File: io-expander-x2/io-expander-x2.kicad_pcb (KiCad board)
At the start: 2 copper layers, 50 x 100 mm, 6 parts, among them IC1 MCP23017-E_SO, IC2 MCP23017-E_SO, J1 CONN4_BM04B-SRSS_JST, J2 CONN4_BM04B-SRSS_JST, J3 Screw-8P-5.08-1729186, J4 Screw-8P-5.08-1729186

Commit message: Daughter board is coming along nicely.
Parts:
- added D1: LED, LED_SMD:LED_1206_3216Metric, F.Cu at (61.1, 43.2)
- added F1: MF-USHT010KX-2, 00_General:FUSC3226X85N, F.Cu at (47.4, 43.2)
- added H1: MountingHole, MountingHole:MountingHole_3.2mm_M3_ISO7380, F.Cu at (45.0, 34.3)
- added H2: MountingHole, MountingHole:MountingHole_3.2mm_M3_ISO7380, F.Cu at (64.8, 34.3)
- added H3: MountingHole, MountingHole:MountingHole_3.2mm_M3_ISO7380, F.Cu at (45.0, 125.7)
- added H4: MountingHole, MountingHole:MountingHole_3.2mm_M3_ISO7380, F.Cu at (64.8, 125.7)
- added J5: Screw-8P-5.08-1729186, 00_Connectors:Screw-8P-5.08-1729186, F.Cu at (36.0, 85.0)
- added J6: Screw-8P-5.08-1729186, 00_Connectors:Screw-8P-5.08-1729186, F.Cu at (73.7, 120.6)
- added R1: R, Resistor_SMD:R_0805_2012Metric, F.Cu at (54.4, 43.2)
- IC1, IC2: footprint 00_General:SOIC127P1030X265-28N -> SamacSys_Parts:SOIC127P1030X265-28N
- moved J2 40.2 mm to (62.8, 80.2)
- moved J3 35.3 mm to (36.0, 39.0)
- moved J4 33.9 mm to (73.7, 73.6)
- moved J1 24.7 mm to (50.1, 80.2), turned to -90 degrees
- moved IC1 22.7 mm to (55.3, 59.0)
- moved IC2 19.8 mm to (55.3, 102.0)
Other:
- board text added: "Port A"
- board text added: "Port B"

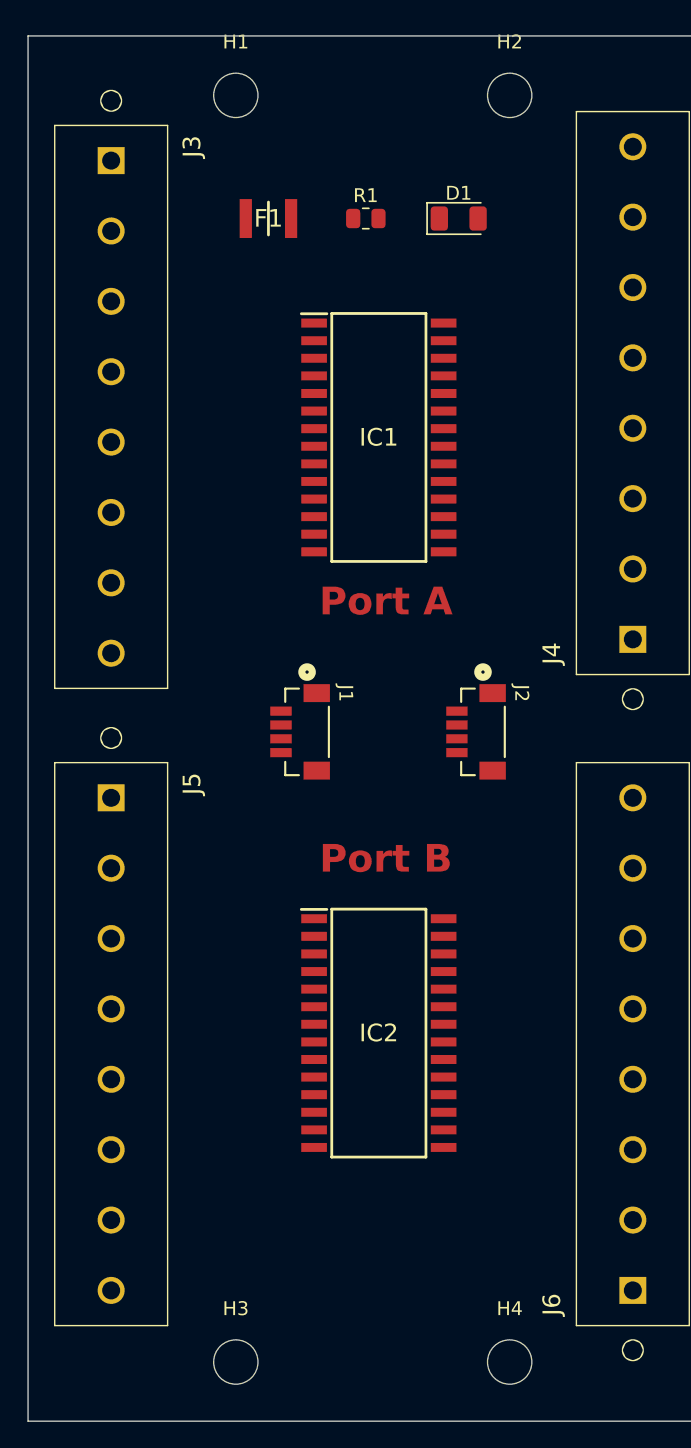
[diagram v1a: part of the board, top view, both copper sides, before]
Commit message: Most components are now placed. The schematic has a lot of the wiring done. Need to transfer it onto the PCB once I figure out how I will wire up the address lines.
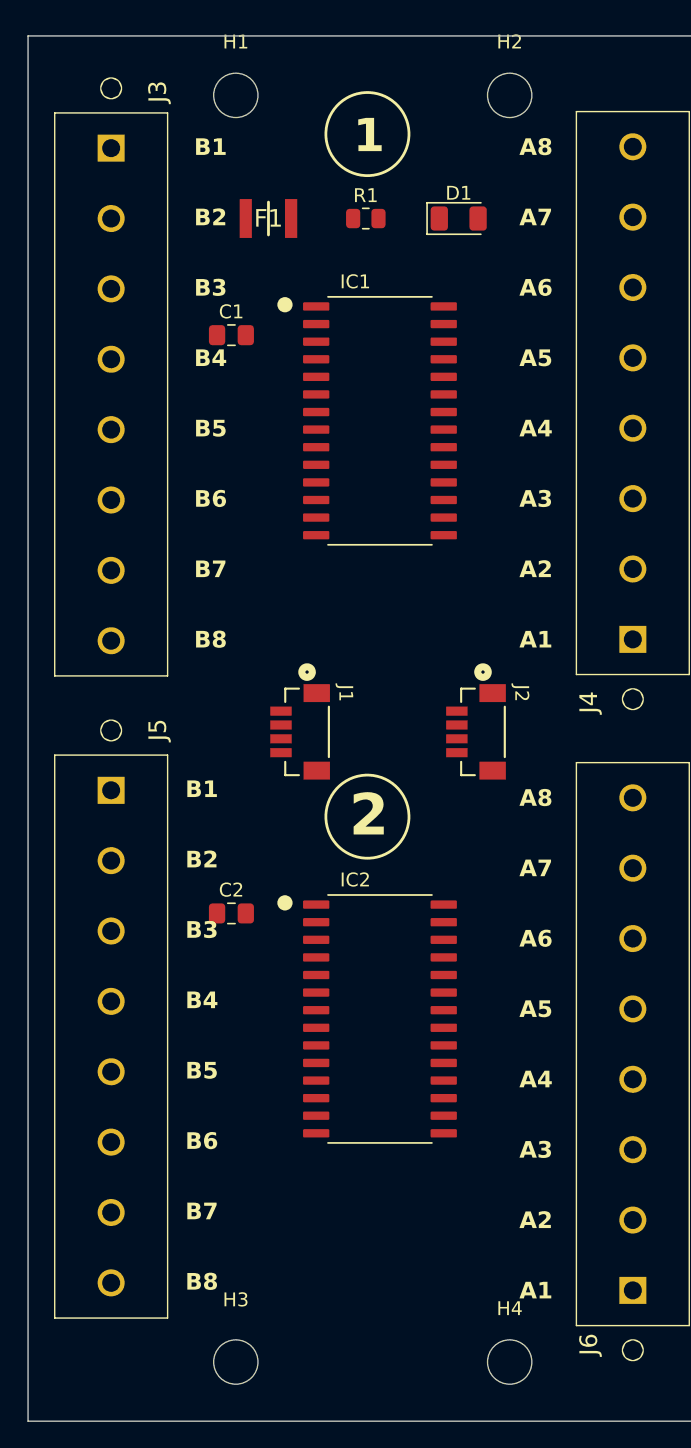
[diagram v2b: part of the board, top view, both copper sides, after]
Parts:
- added C1: C, Capacitor_SMD:C_0805_2012Metric_Pad1.18x1.45mm_HandSolder, F.Cu at (44.7, 51.6)
- added C2: C, Capacitor_SMD:C_0805_2012Metric_Pad1.18x1.45mm_HandSolder, F.Cu at (44.7, 93.3)
- IC1, IC2: footprint SamacSys_Parts:SOIC127P1030X265-28N -> 00_General:MCP23017-E-SO
- J1, J2: value CONN4_BM04B-SRSS_JST -> QWIIC
- moved IC1 1.20 mm to (55.4, 57.8)
- moved IC2 1.02 mm to (55.4, 101.0)
- moved J3 0.90 mm to (36.0, 38.1)
- moved J5 0.55 mm to (36.0, 84.5)
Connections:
- D1 pad 1: unconnected-(D1-K-Pad1) -> GND
- F1 pad 1: unconnected-(F1-Pad1) -> +3V3
- F1 pad 2: unconnected-(F1-Pad2) -> +3V3
- IC1 pad 1: unconnected-(IC1-GPB0-Pad1) -> Net-(IC1-GPB0)
- IC1 pad 10: unconnected-(IC1-VSS-Pad10) -> GND
- IC1 pad 12: unconnected-(IC1-SCL-Pad12) -> /SCK
- IC1 pad 13: unconnected-(IC1-SDA-Pad13) -> /SDA
- IC1 pad 2: unconnected-(IC1-GPB1-Pad2) -> Net-(IC1-GPB1)
- IC1 pad 21: unconnected-(IC1-GPA0-Pad21) -> Net-(IC1-GPA0)
- IC1 pad 22: unconnected-(IC1-GPA1-Pad22) -> Net-(IC1-GPA1)
- IC1 pad 23: unconnected-(IC1-GPA2-Pad23) -> Net-(IC1-GPA2)
- IC1 pad 24: unconnected-(IC1-GPA3-Pad24) -> Net-(IC1-GPA3)
- IC1 pad 25: unconnected-(IC1-GPA4-Pad25) -> Net-(IC1-GPA4)
- IC1 pad 26: unconnected-(IC1-GPA5-Pad26) -> Net-(IC1-GPA5)
- IC1 pad 27: unconnected-(IC1-GPA6-Pad27) -> Net-(IC1-GPA6)
- IC1 pad 28: unconnected-(IC1-GPA7-Pad28) -> Net-(IC1-GPA7)
- IC1 pad 3: unconnected-(IC1-GPB2-Pad3) -> Net-(IC1-GPB2)
- IC1 pad 4: unconnected-(IC1-GPB3-Pad4) -> Net-(IC1-GPB3)
- IC1 pad 5: unconnected-(IC1-GPB4-Pad5) -> Net-(IC1-GPB4)
- IC1 pad 6: unconnected-(IC1-GPB5-Pad6) -> Net-(IC1-GPB5)
- IC1 pad 7: unconnected-(IC1-GPB6-Pad7) -> Net-(IC1-GPB6)
- IC1 pad 8: unconnected-(IC1-GPB7-Pad8) -> Net-(IC1-GPB7)
- IC1 pad 9: unconnected-(IC1-VDD-Pad9) -> +3V3
- IC2 pad 1: unconnected-(IC2-GPB0-Pad1) -> Net-(IC2-GPB0)
- IC2 pad 10: unconnected-(IC2-VSS-Pad10) -> GND
- IC2 pad 12: unconnected-(IC2-SCL-Pad12) -> /SCK
- IC2 pad 13: unconnected-(IC2-SDA-Pad13) -> /SDA
- IC2 pad 2: unconnected-(IC2-GPB1-Pad2) -> Net-(IC2-GPB1)
- IC2 pad 21: unconnected-(IC2-GPA0-Pad21) -> Net-(IC2-GPA0)
- IC2 pad 22: unconnected-(IC2-GPA1-Pad22) -> Net-(IC2-GPA1)
- IC2 pad 23: unconnected-(IC2-GPA2-Pad23) -> Net-(IC2-GPA2)
- IC2 pad 24: unconnected-(IC2-GPA3-Pad24) -> Net-(IC2-GPA3)
- IC2 pad 25: unconnected-(IC2-GPA4-Pad25) -> Net-(IC2-GPA4)
- IC2 pad 26: unconnected-(IC2-GPA5-Pad26) -> Net-(IC2-GPA5)
- IC2 pad 27: unconnected-(IC2-GPA6-Pad27) -> Net-(IC2-GPA6)
- IC2 pad 28: unconnected-(IC2-GPA7-Pad28) -> Net-(IC2-GPA7)
- IC2 pad 3: unconnected-(IC2-GPB2-Pad3) -> Net-(IC2-GPB2)
- IC2 pad 4: unconnected-(IC2-GPB3-Pad4) -> Net-(IC2-GPB3)
- IC2 pad 5: unconnected-(IC2-GPB4-Pad5) -> Net-(IC2-GPB4)
- IC2 pad 6: unconnected-(IC2-GPB5-Pad6) -> Net-(IC2-GPB5)
- IC2 pad 7: unconnected-(IC2-GPB6-Pad7) -> Net-(IC2-GPB6)
- IC2 pad 8: unconnected-(IC2-GPB7-Pad8) -> Net-(IC2-GPB7)
- IC2 pad 9: unconnected-(IC2-VDD-Pad9) -> +3V3
- J1 pad 1: unconnected-(J1-GND-Pad1) -> GND
- J1 pad 2: unconnected-(J1-3.3V-Pad2) -> +3V3
- J1 pad 3: unconnected-(J1-SDA-Pad3) -> /SDA
- J1 pad 4: unconnected-(J1-SCK-Pad4) -> /SCK
- J2 pad 1: unconnected-(J2-GND-Pad1) -> GND
- J2 pad 2: unconnected-(J2-3.3V-Pad2) -> +3V3
- J2 pad 3: unconnected-(J2-SDA-Pad3) -> /SDA
- J2 pad 4: unconnected-(J2-SCK-Pad4) -> /SCK
- J3 pad 1: unconnected-(J3-Pad1) -> Net-(IC1-GPB0)
- J3 pad 2: unconnected-(J3-Pad2) -> Net-(IC1-GPB1)
- J3 pad 3: unconnected-(J3-Pad3) -> Net-(IC1-GPB2)
- J3 pad 4: unconnected-(J3-Pad4) -> Net-(IC1-GPB3)
- J3 pad 5: unconnected-(J3-Pad5) -> Net-(IC1-GPB4)
- J3 pad 6: unconnected-(J3-Pad6) -> Net-(IC1-GPB5)
- J3 pad 7: unconnected-(J3-Pad7) -> Net-(IC1-GPB6)
- J3 pad 8: unconnected-(J3-Pad8) -> Net-(IC1-GPB7)
- J4 pad 1: unconnected-(J4-Pad1) -> Net-(IC1-GPA0)
- J4 pad 2: unconnected-(J4-Pad2) -> Net-(IC1-GPA1)
- J4 pad 3: unconnected-(J4-Pad3) -> Net-(IC1-GPA2)
- J4 pad 4: unconnected-(J4-Pad4) -> Net-(IC1-GPA3)
- J4 pad 5: unconnected-(J4-Pad5) -> Net-(IC1-GPA4)
- J4 pad 6: unconnected-(J4-Pad6) -> Net-(IC1-GPA5)
- J4 pad 7: unconnected-(J4-Pad7) -> Net-(IC1-GPA6)
- J4 pad 8: unconnected-(J4-Pad8) -> Net-(IC1-GPA7)
- J5 pad 1: unconnected-(J5-Pad1) -> Net-(IC2-GPB0)
- J5 pad 2: unconnected-(J5-Pad2) -> Net-(IC2-GPB1)
- J5 pad 3: unconnected-(J5-Pad3) -> Net-(IC2-GPB2)
- J5 pad 4: unconnected-(J5-Pad4) -> Net-(IC2-GPB3)
- J5 pad 5: unconnected-(J5-Pad5) -> Net-(IC2-GPB4)
- J5 pad 6: unconnected-(J5-Pad6) -> Net-(IC2-GPB5)
- J5 pad 7: unconnected-(J5-Pad7) -> Net-(IC2-GPB6)
- J5 pad 8: unconnected-(J5-Pad8) -> Net-(IC2-GPB7)
- J6 pad 1: unconnected-(J6-Pad1) -> Net-(IC2-GPA0)
- J6 pad 2: unconnected-(J6-Pad2) -> Net-(IC2-GPA1)
- J6 pad 3: unconnected-(J6-Pad3) -> Net-(IC2-GPA2)
- J6 pad 4: unconnected-(J6-Pad4) -> Net-(IC2-GPA3)
- J6 pad 5: unconnected-(J6-Pad5) -> Net-(IC2-GPA4)
- J6 pad 6: unconnected-(J6-Pad6) -> Net-(IC2-GPA5)
- J6 pad 7: unconnected-(J6-Pad7) -> Net-(IC2-GPA6)
- J6 pad 8: unconnected-(J6-Pad8) -> Net-(IC2-GPA7)
- R1 pad 1: unconnected-(R1-Pad1) -> Net-(D1-A)
- R1 pad 2: Net-(D1-A) -> +3V3
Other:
- board text added: "1"
- board text added: "2"
- board text added: "A1"
- board text added: "A2"
- board text added: "A3"
- board text added: "A4"
- board text added: "A5"
- board text added: "A6"
- board text added: "A7"
- board text added: "A8"
- board text added: "B1"
- board text added: "B2"
- board text added: "B3"
- board text added: "B4"
- board text added: "B5"
- board text added: "B6"
- board text added: "B7"
- board text added: "B8"
- board text removed: "Port A"
- board text removed: "Port B"

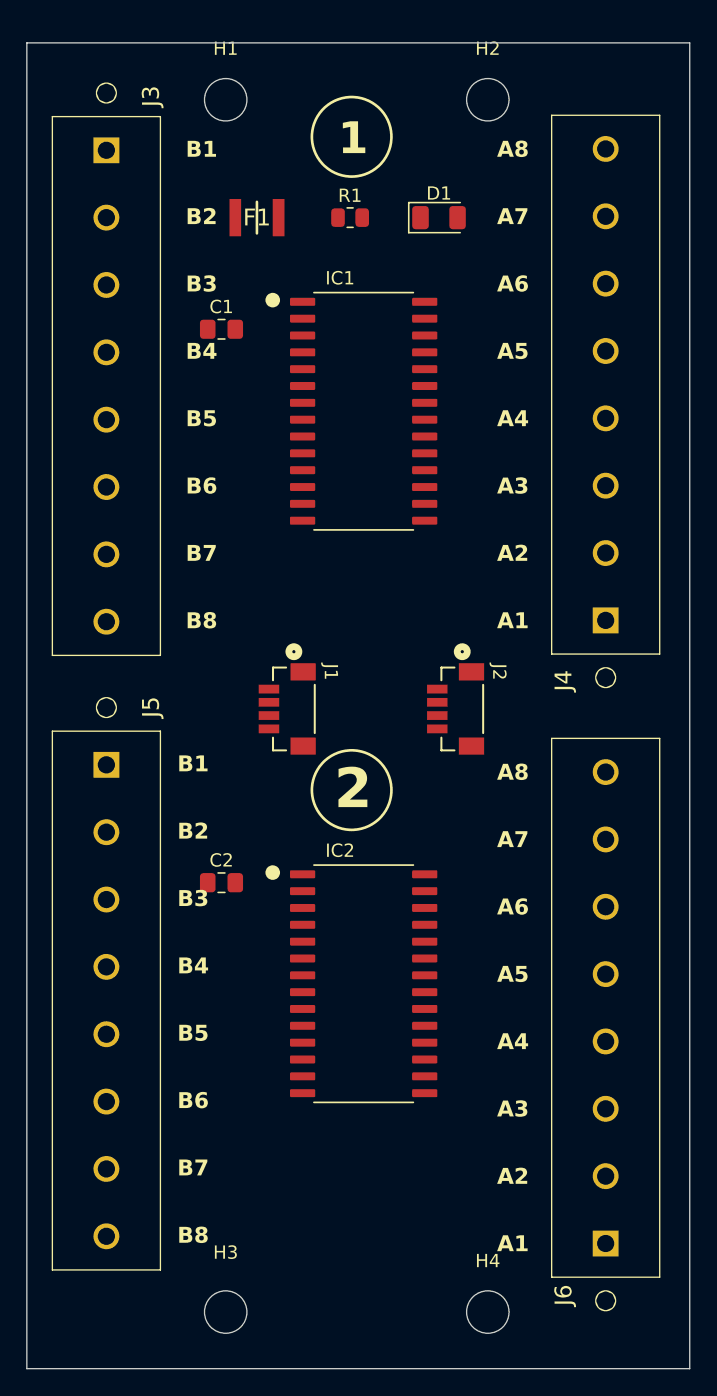
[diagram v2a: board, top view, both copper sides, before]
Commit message: Added ground connectors. Board is overly tight now.
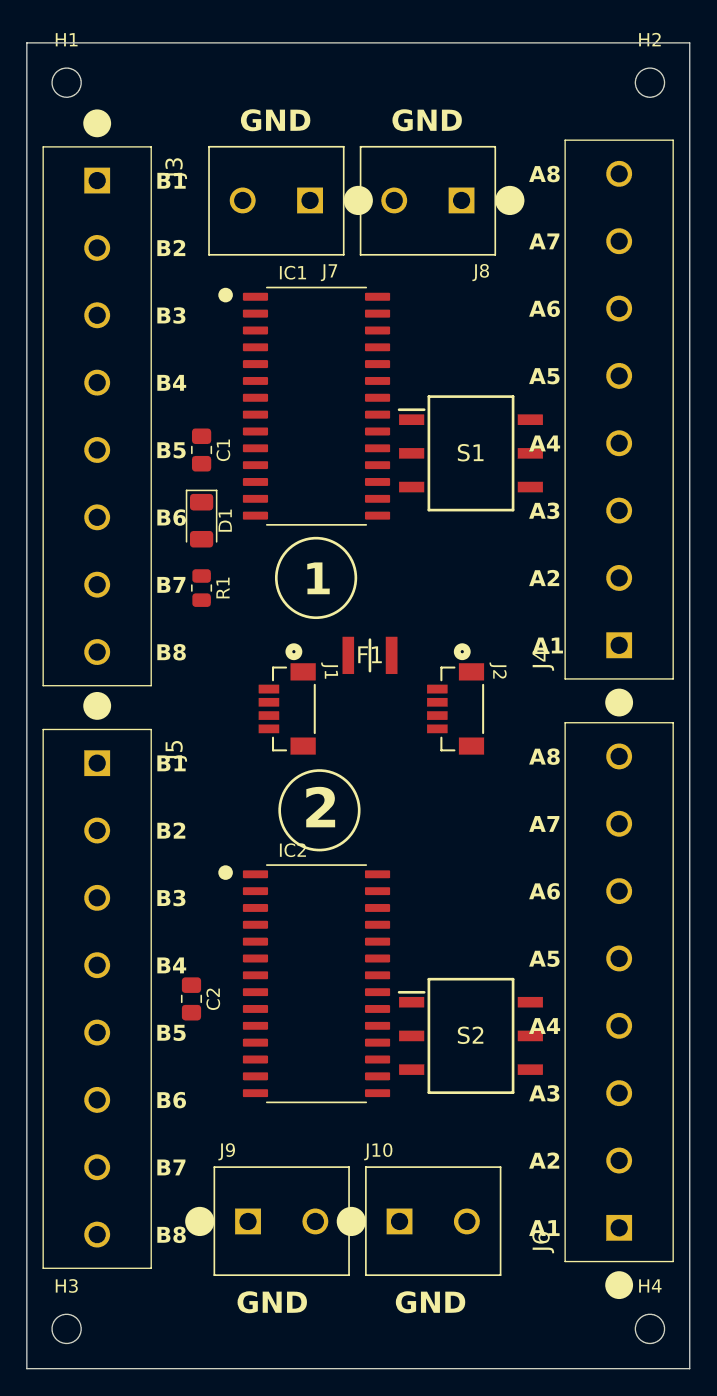
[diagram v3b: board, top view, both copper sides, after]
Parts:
- added J10: Screw-2P-5.08-1729128, 00_Connectors:Screw-2P-5.08-1729128, F.Cu at (55.6, 122.9)
- added J7: Screw-2P-5.08-1729128, 00_Connectors:Screw-2P-5.08-1729128, F.Cu at (53.9, 37.8)
- added J8: Screw-2P-5.08-1729128, 00_Connectors:Screw-2P-5.08-1729128, F.Cu at (65.3, 37.8)
- added J9: Screw-2P-5.08-1729128, 00_Connectors:Screw-2P-5.08-1729128, F.Cu at (44.1, 122.9)
- added S1: 418121160803, 00_General:SOP254P980X300-6N, F.Cu at (63.5, 61.0)
- added S2: 418121160803, 00_General:SOP254P980X300-6N, F.Cu at (63.5, 104.9)
- H1, H2, H3, H4: footprint MountingHole:MountingHole_3.2mm_M3_ISO7380 -> MountingHole:MountingHole_2.2mm_M2
- moved F1 34.1 mm to (55.9, 76.2)
- moved R1 30.1 mm to (43.2, 71.1), turned to -90 degrees
- moved D1 29.0 mm to (43.2, 66.0), turned to -90 degrees
- moved H2 12.3 mm to (77.0, 33.0)
- moved H4 12.3 mm to (77.0, 127.0)
- moved H1 12.1 mm to (33.0, 33.0)
- moved H3 12.1 mm to (33.0, 127.0)
- moved C1 9.23 mm to (43.2, 60.7), turned to -90 degrees
- moved C2 9.05 mm to (42.4, 102.1), turned to -90 degrees
- moved IC1 3.58 mm to (51.8, 57.4)
- moved IC2 3.56 mm to (51.8, 101.0)
- moved J3 2.39 mm to (35.3, 40.4)
- moved J4 2.14 mm to (74.7, 75.4)
- moved J6 1.56 mm to (74.7, 119.4)
- moved J5 0.71 mm to (35.3, 84.3)
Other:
- board text added: "GND"

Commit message: Going to use 3x3 header block instead.
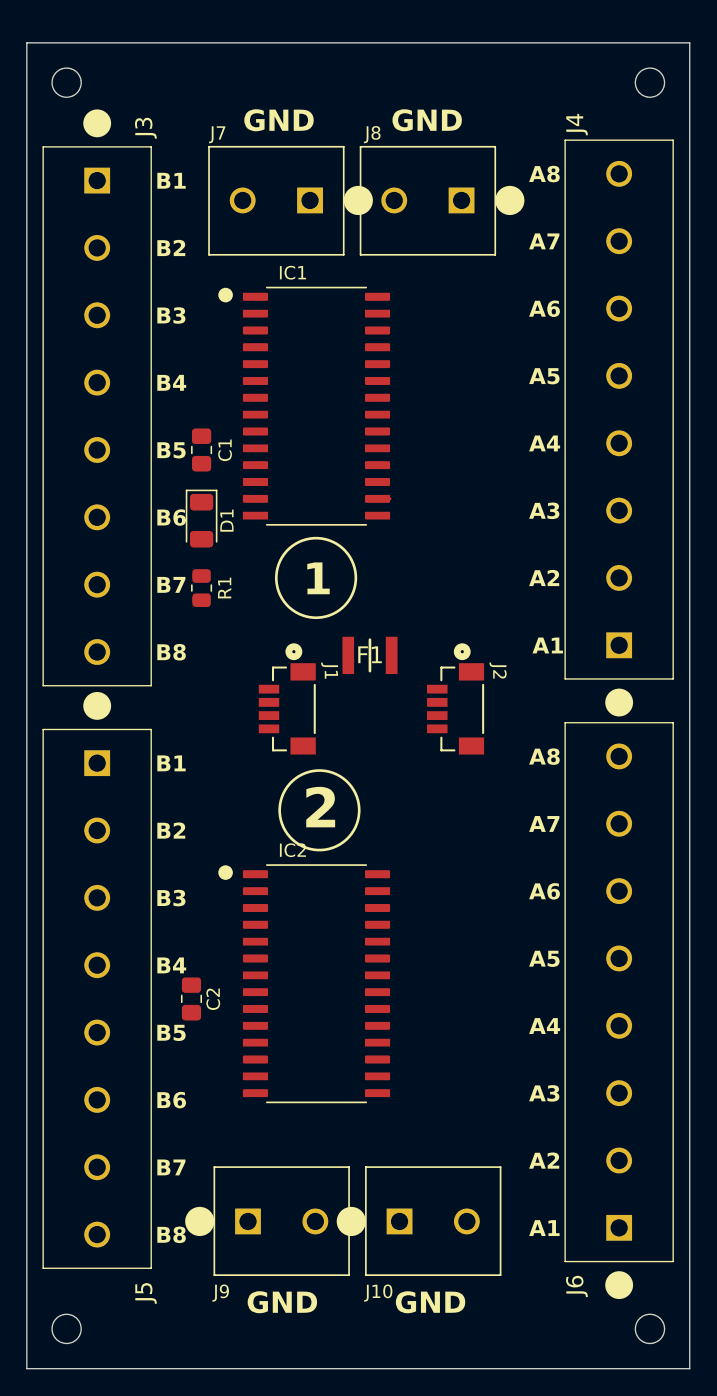
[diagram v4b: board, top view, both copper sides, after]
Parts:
- removed S1, S2: 418121160803, 00_General:SOP254P980X300-6N
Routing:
- net unconnected-(IC1-A1-Pad16): track 0.00 -> 0.95 mm

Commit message: Minor changes.
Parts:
- removed J10, J7, J8, J9: Screw-2P-5.08-1729128, 00_Connectors:Screw-2P-5.08-1729128
- F1: footprint 00_General:FUSC3226X85N -> 00_general:FUSC3226X85N
- IC1, IC2: footprint 00_General:MCP23017-E-SO -> 00_general:MCP23017-E-SO
- J1, J2: value QWIIC -> CONN4_BM04B-SRSS_JST; footprint 00_Connectors:QWIIC -> 00_connectors:QWIIC
- J3, J4, J5, J6: value Screw-8P-5.08-1729186 -> 8 Position Screw Terminal; footprint 00_Connectors:Screw-8P-5.08-1729186 -> 00_connectors:PHOENIX_1869279
- moved J4 8.07 mm to (79.7, 81.8)
- moved J6 7.48 mm to (79.7, 125.0)
- moved J5 4.42 mm to (32.1, 81.3)
- moved J3 3.22 mm to (32.1, 40.1)
